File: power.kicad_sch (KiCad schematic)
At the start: 0 parts

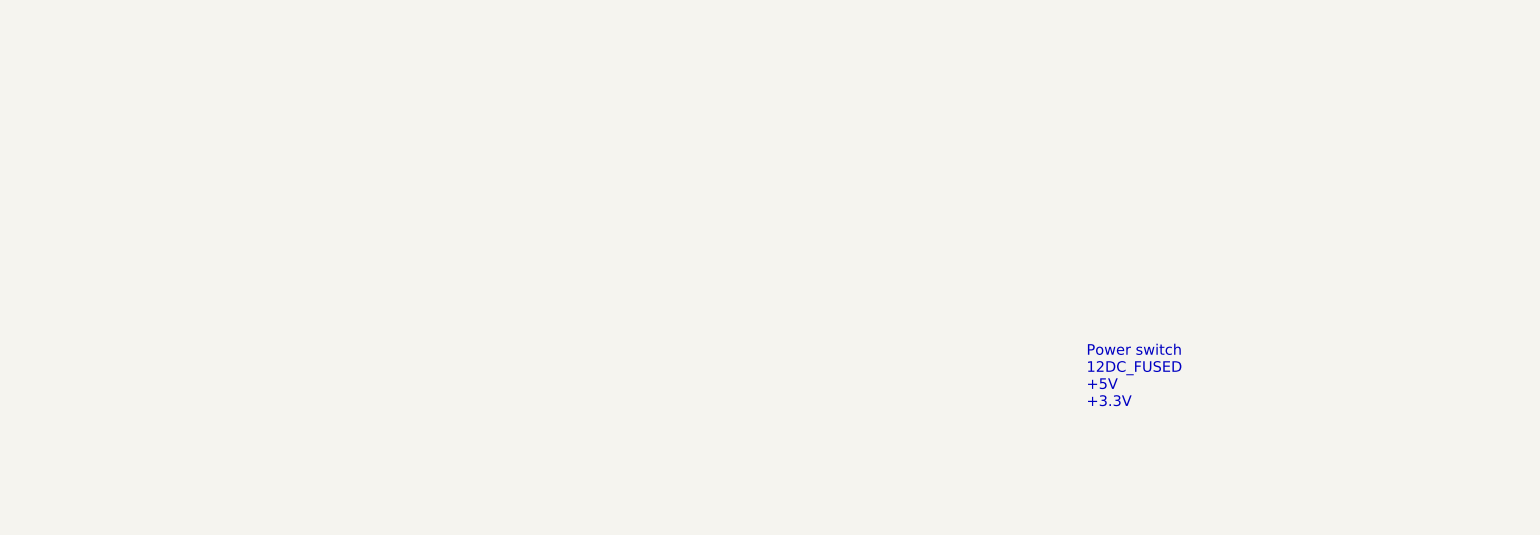
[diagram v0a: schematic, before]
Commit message: finish implementing 5V power supply
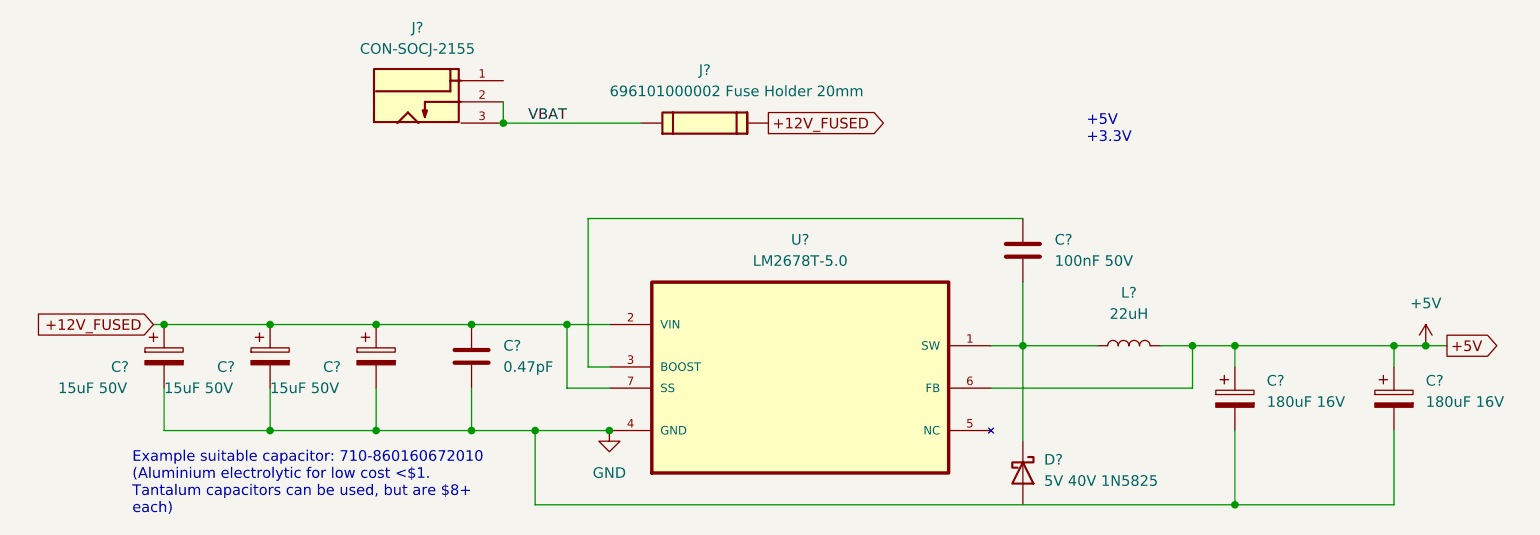
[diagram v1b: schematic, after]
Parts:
- added C? (x3): 15uF 50V, Capacitor_THT:CP_Radial_D5.0mm_P2.00mm, symbol Device:C_Polarized
- added C?: 100nF 50V, symbol Device:C
- added C? (x2): 180uF 16V, Capacitor_THT:CP_Radial_D10.0mm_P5.00mm, symbol Device:C_Polarized
- added C?: 0.47pF, symbol Device:C
- added D?: 5V 40V 1N5825, Diode_THT:D_5KP_P12.70mm_Horizontal, symbol Device:D_Schottky
- added J?: CON-SOCJ-2155, GRAVITECH_CON-SOCJ-2155, symbol 00Project-SOCJ-2155:CON-SOCJ-2155
- added J?: 696101000002 Fuse Holder 20mm, 696101000002, symbol 00Project-FuseHolder:696101000002
- added L?: 22uH, symbol Device:L
- added U?: LM2678T-5.0, TO127P457X1016X2052-7P, symbol 00Project-5VReg:LM2678T-5.0
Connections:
- new net: C?.2, D?.1 (K), L?.1, U?.1 (SW)
- new net: C?.1, U?.3 (BOOST)
- new net +12V_FUSED: C?.1, C?.1, C?.1, C?.1, J?.2, U?.2 (VIN), U?.7 (SS)
- new net +5V: C?.1, C?.1, L?.2, U?.6 (FB)
- new net GND: C?.2, C?.2, C?.2, C?.2, C?.2, C?.2, U?.4 (GND)
- new net VBAT: J?.1, J?.2, J?.3
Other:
- note added: "+5V +3.3V"
- note added: "Example suitable capacitor: 710-860160672010 (Aluminium electrolytic for low cost <$1. Tantalum capacitors can be used, but are $8+ each)"
- note removed: "Power switch 12DC_FUSED +5V +3.3V"

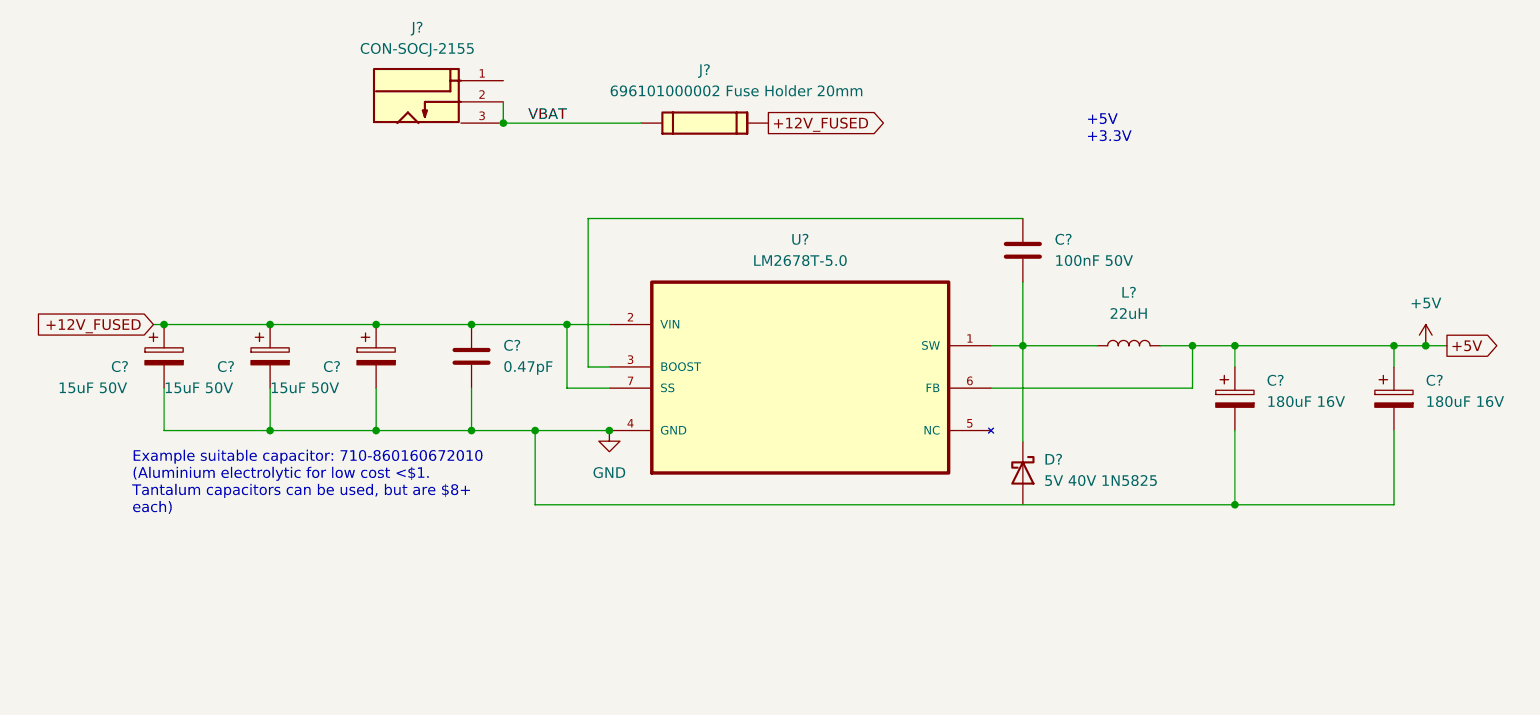
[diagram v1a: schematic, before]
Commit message: add header for +5V to QMTECH WUKONG FPGA board
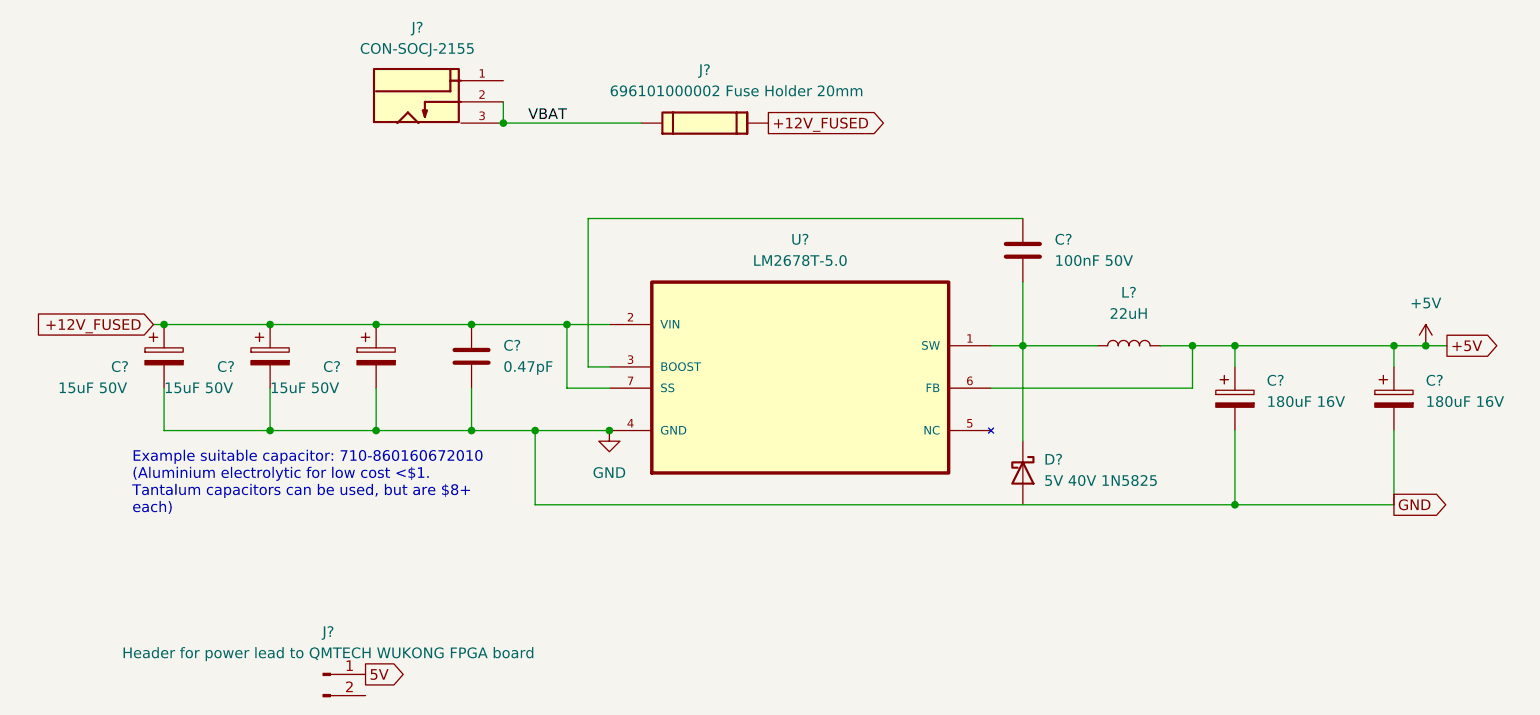
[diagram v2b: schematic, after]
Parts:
- added J?: Header for power lead to QMTECH WUKONG FPGA board, symbol Connector:Conn_01x02_Male
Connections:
- new net 5V: J?.1 (Pin_1)
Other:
- note removed: "+5V +3.3V"
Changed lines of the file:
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@@
-    (effects (font (size 1.27 1.27)) (justify left bottom))
-  )
-  (text "+5V\n+3.3V" (at 139.7 67.31 0)
     (effects (font (size 1.27 1.27)) (justify left bottom))
   )
@@
     (effects (font (size 1.27 1.27)) (justify left))
     (property "Intersheet References" "${INTERSHEET_REFS}" (id 0) (at 189.1636 91.3606 0)
+      (effects (font (size 1.27 1.27)) (justify left) hide)
+    )
+  )
+  (global_label "GND" (shape output) (at 176.53 110.49 0) (fields_autoplaced)
+    (effects (font (size 1.27 1.27)) (justify left))
+    (property "Intersheet References" "${INTERSHEET_REFS}" (id 0) (at 182.8136 110.4106 0)
       (effects (font (size 1.27 1.27)) (justify left) hide)
     )
@@
     (effects (font (size 1.27 1.27)) (justify left))
     (property "Intersheet References" "${INTERSHEET_REFS}" (id 0) (at 116.1083 64.6906 0)
+      (effects (font (size 1.27 1.27)) (justify left) hide)
+    )
+  )
+  (global_label "5V" (shape output) (at 53.34 130.81 0) (fields_autoplaced)
+    (effects (font (size 1.27 1.27)) (justify left))
+    (property "Intersheet References" "${INTERSHEET_REFS}" (id 0) (at 58.0512 130.7306 0)
       (effects (font (size 1.27 1.27)) (justify left) hide)
     )
@@
     (pin "1")
   )
+  (symbol (lib_id "Connector:Conn_01x02_Male") (at 48.26 130.81 0) (unit 1)
+    (in_bom yes) (on_board yes) (fields_autoplaced)
+    (property "Reference" "J?" (id 0) (at 48.895 125.73 0))
+    (property "Value" "Header for power lead to QMTECH WUKONG FPGA board" (id 1) (at 48.895 128.27 0))
+    (property "Footprint" "" (id 2) (at 48.26 130.81 0)
+      (effects (font (size 1.27 1.27)) hide)
+    )
+    (property "Datasheet" "~" (id 3) (at 48.26 130.81 0)
+      (effects (font (size 1.27 1.27)) hide)
+    )
+    (pin "1")
+    (pin "2")
+  )
   (symbol (lib_id "Device:C_Polarized") (at 157.48 97.79 0) (unit 1)

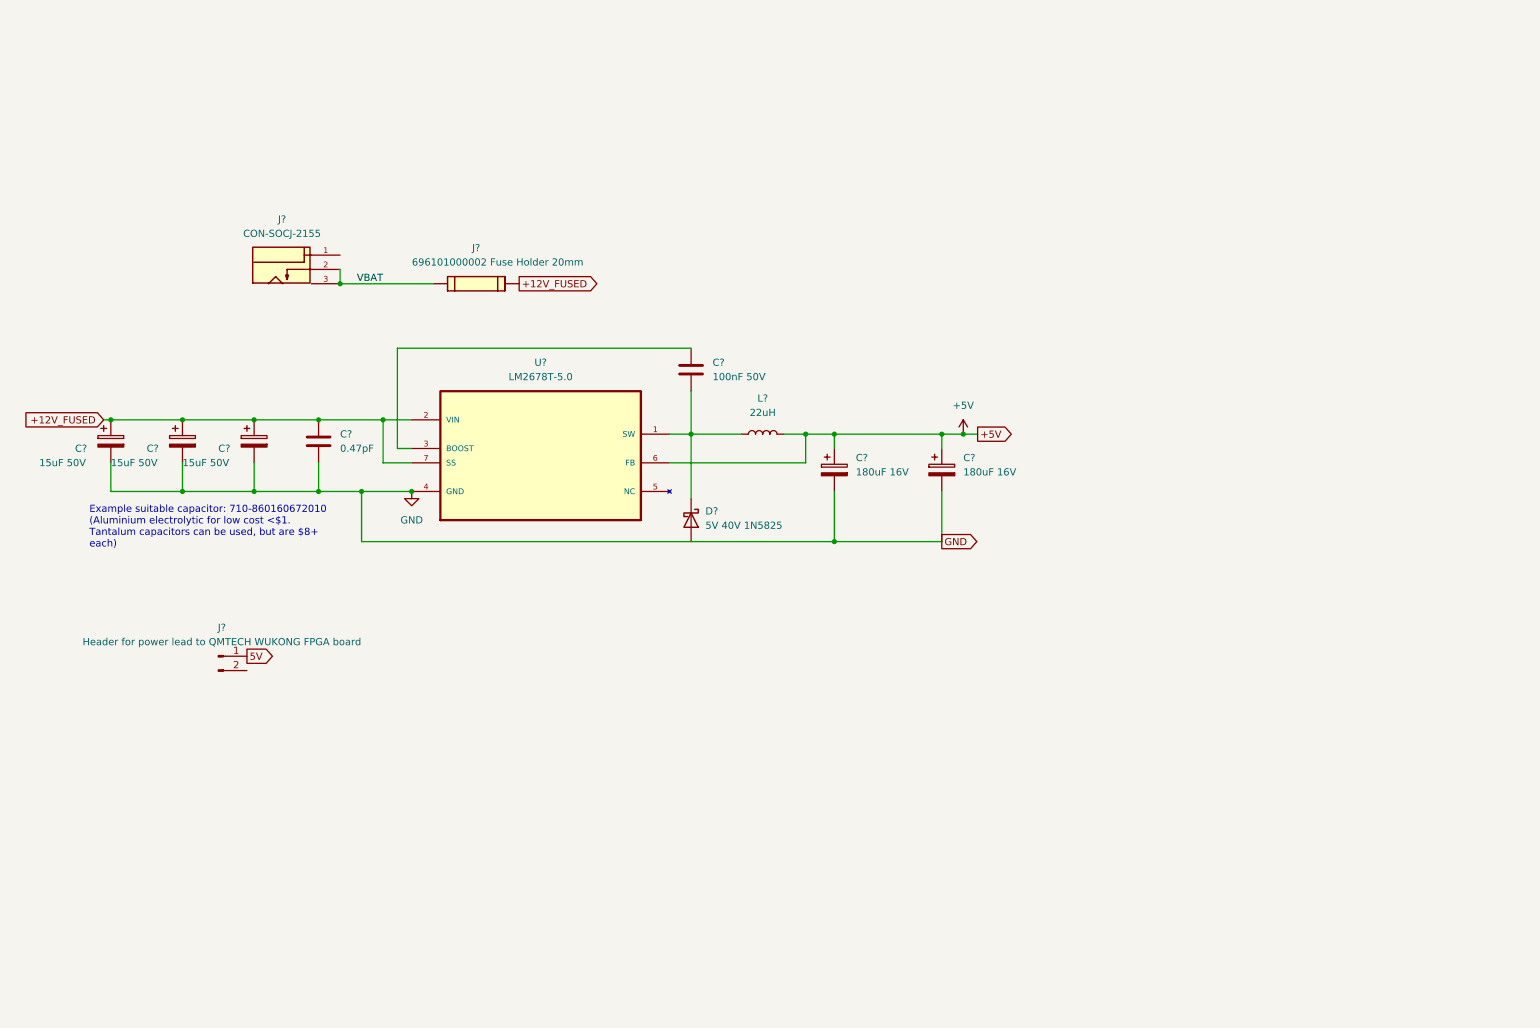
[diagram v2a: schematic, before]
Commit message: beautify the schematics, especially the title-page
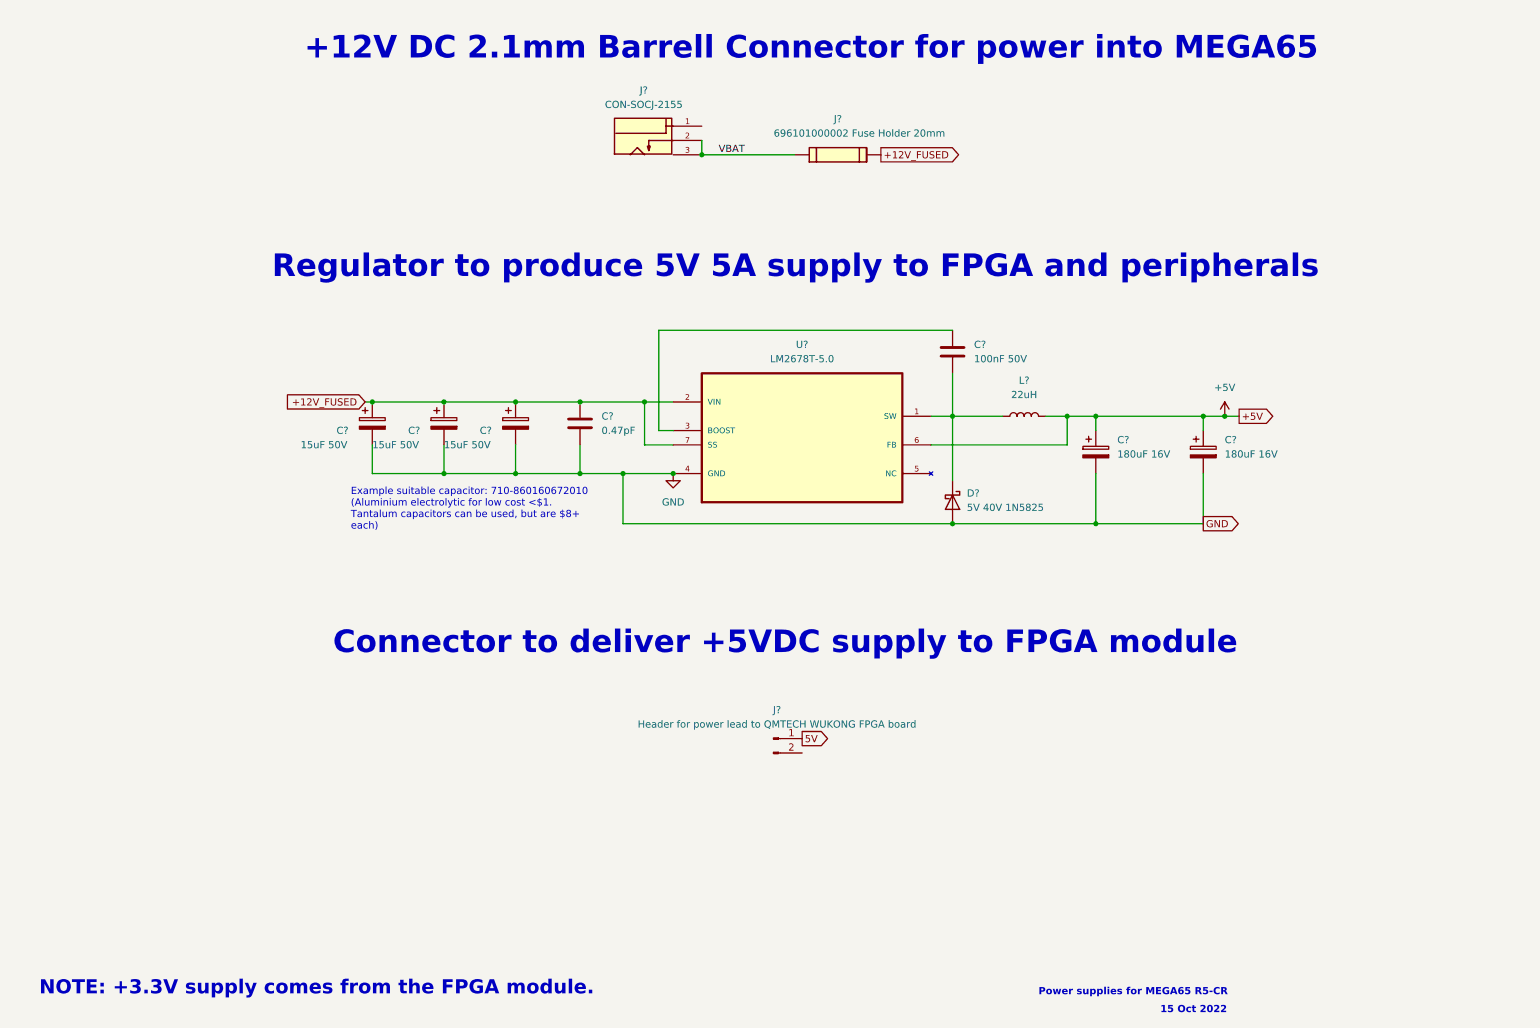
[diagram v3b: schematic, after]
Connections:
- net GND: now also D?.2 (A)
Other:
- note added: "+12V DC 2.1mm Barrell Connector for power into MEGA65"
- note added: "15 Oct 2022"
- note added: "Connector to deliver +5VDC supply to FPGA module"
- note added: "NOTE: +3.3V supply comes from the FPGA module."
- note added: "Power supplies for MEGA65 R5-CR"
- note added: "Regulator to produce 5V 5A supply to FPGA and peripherals"
- moved on the sheet: C?, D?, J?, L?, U?
